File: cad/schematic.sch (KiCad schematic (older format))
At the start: 5 parts

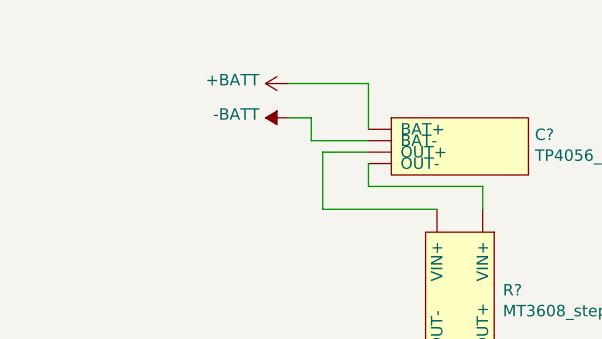
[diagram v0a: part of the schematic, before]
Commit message: Adds switch to schematic
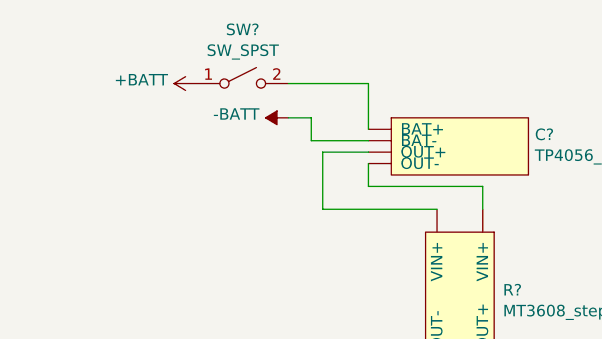
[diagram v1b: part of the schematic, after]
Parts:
- added SW?: SW_SPST, symbol Switch:SW_SPST
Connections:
- net +BATT: now also SW?.1 (A); no longer C?.~ (OUT-)
- new net: C?.~ (OUT-), R?.~ (VOUT-)
- new net: C?.~ (OUT-), SW?.2 (B)
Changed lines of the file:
@@
 L power:+BATT #PWR?
 U 1 1 61907218
-P 4450 2350
-F 0 "#PWR?" H 4450 2200 50  0001 C CNN
-F 1 "+BATT" V 4465 2477 50  0000 L CNN
-F 2 "" H 4450 2350 50  0001 C CNN
-F 3 "" H 4450 2350 50  0001 C CNN
-	1    4450 2350
+P 4050 2350
+F 0 "#PWR?" H 4050 2200 50  0001 C CNN
+F 1 "+BATT" V 4065 2477 50  0000 L CNN
+F 2 "" H 4050 2350 50  0001 C CNN
+F 3 "" H 4050 2350 50  0001 C CNN
+	1    4050 2350
 	0    -1   -1   0
 $EndComp
@@
 Wire Wire Line
 	5150 6100 5150 6700
+$Comp
+L Switch:SW_SPST SW?
+U 1 1 61908D6C
+P 4250 2350
+F 0 "SW?" H 4250 2585 50  0000 C CNN
+F 1 "SW_SPST" H 4250 2494 50  0000 C CNN
+F 2 "" H 4250 2350 50  0001 C CNN
+F 3 "~" H 4250 2350 50  0001 C CNN
+	1    4250 2350
+	1    0    0    -1
+$EndComp
 $EndSCHEMATC

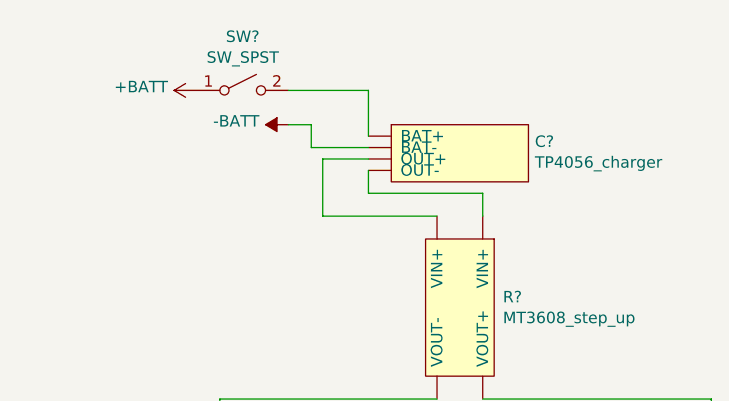
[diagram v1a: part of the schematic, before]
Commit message: Updates switch position in schematic
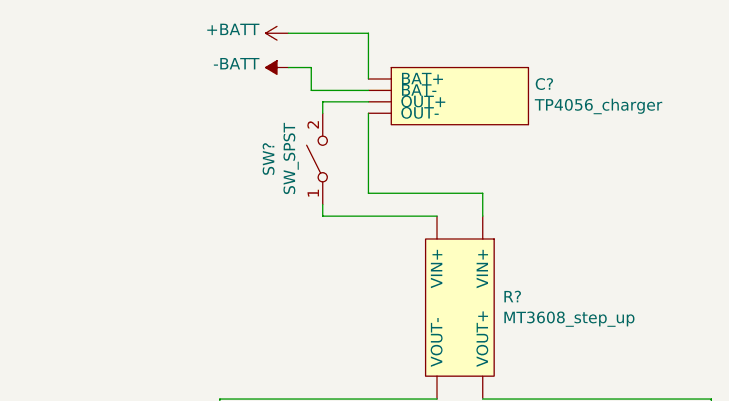
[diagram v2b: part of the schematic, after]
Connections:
- net +BATT: now also C?.~ (OUT-); no longer SW?.1 (A)
- net at R?.~ (VOUT-): now also SW?.1 (A); no longer C?.~ (OUT-)
- new net: C?.~ (OUT-), R?.~ (VOUT-)
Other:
- moved on the sheet: C?, SW?
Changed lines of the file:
@@
 L CoffeScale:TP4056_charger C?
 U 1 1 618F0B85
-P 5200 2450
-F 0 "C?" H 5528 2326 50  0000 L CNN
-F 1 "TP4056_charger" H 5528 2235 50  0000 L CNN
-F 2 "" H 5200 2450 50  0001 C CNN
-F 3 "" H 5200 2450 50  0001 C CNN
-	1    5200 2450
+P 5200 2200
+F 0 "C?" H 5528 2076 50  0000 L CNN
+F 1 "TP4056_charger" H 5528 1985 50  0000 L CNN
+F 2 "" H 5200 2200 50  0001 C CNN
+F 3 "" H 5200 2200 50  0001 C CNN
+	1    5200 2200
 	1    0    0    -1
 $EndComp
@@
 $EndComp
 Wire Wire Line
-	4800 2650 4600 2650
-Wire Wire Line
-	4600 2650 4600 2900
+	4800 2400 4600 2400
 Wire Wire Line
 	4600 2900 5100 2900
-Wire Wire Line
-	4800 2700 4800 2800
 Wire Wire Line
 	4800 2800 5300 2800
@@
 L power:+BATT #PWR?
 U 1 1 61907218
-P 4050 2350
-F 0 "#PWR?" H 4050 2200 50  0001 C CNN
-F 1 "+BATT" V 4065 2477 50  0000 L CNN
-F 2 "" H 4050 2350 50  0001 C CNN
-F 3 "" H 4050 2350 50  0001 C CNN
-	1    4050 2350
-	0    -1   -1   0
-$EndComp
-$Comp
-L power:-BATT #PWR?
-U 1 1 61908632
-P 4450 2500
-F 0 "#PWR?" H 4450 2350 50  0001 C CNN
-F 1 "-BATT" V 4465 2627 50  0000 L CNN
-F 2 "" H 4450 2500 50  0001 C CNN
-F 3 "" H 4450 2500 50  0001 C CNN
-	1    4450 2500
+P 4450 2100
+F 0 "#PWR?" H 4450 1950 50  0001 C CNN
+F 1 "+BATT" V 4465 2227 50  0000 L CNN
+F 2 "" H 4450 2100 50  0001 C CNN
+F 3 "" H 4450 2100 50  0001 C CNN
+	1    4450 2100
 	0    -1   -1   0
 $EndComp
 Wire Wire Line
-	4550 2500 4550 2600
+	4550 2250 4550 2350
 Wire Wire Line
-	4550 2600 4800 2600
+	4550 2350 4800 2350
 Wire Wire Line
-	4800 2350 4800 2550
+	4800 2100 4800 2300
 Wire Wire Line
-	4550 2500 4450 2500
+	4550 2250 4450 2250
 Wire Wire Line
-	4450 2350 4800 2350
+	4450 2100 4800 2100
 $Comp
 L power:GND #PWR?
@@
 L Switch:SW_SPST SW?
 U 1 1 61908D6C
-P 4250 2350
-F 0 "SW?" H 4250 2585 50  0000 C CNN
-F 1 "SW_SPST" H 4250 2494 50  0000 C CNN
-F 2 "" H 4250 2350 50  0001 C CNN
-F 3 "~" H 4250 2350 50  0001 C CNN
-	1    4250 2350
-	1    0    0    -1
+P 4600 2650
+F 0 "SW?" H 4600 2885 50  0000 C CNN
+F 1 "SW_SPST" H 4600 2794 50  0000 C CNN
+F 2 "" H 4600 2650 50  0001 C CNN
+F 3 "~" H 4600 2650 50  0001 C CNN
+	1    4600 2650
+	0    -1   -1   0
 $EndComp
+$Comp
+L power:-BATT #PWR?
+U 1 1 61908632
+P 4450 2250
+F 0 "#PWR?" H 4450 2100 50  0001 C CNN
+F 1 "-BATT" V 4465 2377 50  0000 L CNN
+F 2 "" H 4450 2250 50  0001 C CNN
+F 3 "" H 4450 2250 50  0001 C CNN
+	1    4450 2250
+	0    -1   -1   0
+$EndComp
+Wire Wire Line
+	4600 2900 4600 2850
+Wire Wire Line
+	4600 2450 4600 2400
+Wire Wire Line
+	4800 2450 4800 2800
 $EndSCHEMATC
